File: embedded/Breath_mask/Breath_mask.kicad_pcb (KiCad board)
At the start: 2 copper layers, 38 parts, among them IC1 TPS61291DRVR, J2 USB, J4 Conn_ST_STDC14, SW2 SW_Push, SW3 SW_Push, U1 LPS22HBTR, U23 M95256, U4 STM32L052K8Tx

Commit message: Aggiornamento sbroglio
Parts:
- added G***: LOGO, LOGO, B.Cu at (115.8, 87.8)
- moved TP1 47.8 mm to (137.5, 48.2)
- moved J4 47.1 mm to (147.1, 61.4), turned to 90 degrees
- moved R10 44.4 mm to (117.0, 83.5), turned to 180 degrees
- moved R9 40.6 mm to (120.5, 79.3), turned to -90 degrees
- moved R8 39.4 mm to (117.0, 86.8)
- moved C3 38.9 mm to (126.5, 64.3), turned to -90 degrees
- moved SW3 38.1 mm to (122.8, 73.0)
- moved C11 35.7 mm to (117.0, 79.8)
- moved C8 35.4 mm to (117.8, 74.5), turned to -90 degrees
- moved C6 32.0 mm to (134.8, 63.5), turned to 90 degrees
- moved R7 31.7 mm to (131.8, 64.3)
- moved R15 31.0 mm to (130.0, 80.6), turned to -90 degrees
- moved R12 28.5 mm to (132.0, 80.6), turned to -90 degrees
- moved C4 27.1 mm to (126.6, 68.6)
- moved C5 27.1 mm to (133.3, 60.0)
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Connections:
- SW2 pad 3: (no net) -> GND
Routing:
- net +3V3: track 5.31 -> 178.0 mm
- net Net-(BT1-+): track 0.00 -> 56.5 mm
- net /SENS_CS: track 0.00 -> 41.9 mm, vias 0 -> 4
- net /~{RST}: track 0.00 -> 40.1 mm, vias 0 -> 2
- net /USB_F: track 0.00 -> 32.5 mm, vias 0 -> 2
- net /SPI1_SCK: track 0.00 -> 30.6 mm, vias 0 -> 4
- net /USART1_RX: track 0.00 -> 27.6 mm, vias 0 -> 2
- net /SPI1_MOSI: track 0.00 -> 26.4 mm
- net /SPI1_MISO: track 0.00 -> 24.4 mm, vias 0 -> 2
- net /INTERRUPT_SENS: track 0.00 -> 23.3 mm, vias 0 -> 2
- net Net-(IC1-VIN): track 0.00 -> 21.4 mm, vias 0 -> 2
- net Net-(J2-VBUS-PadA4): track 0.00 -> 20.4 mm
- net /USART1_TX: track 0.00 -> 20.3 mm, vias 0 -> 2
- net Net-(J2-CC2): track 0.00 -> 17.4 mm, vias 0 -> 2
- net /MEM_CS: track 0.00 -> 16.8 mm
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- added copper zone on B.Cu, net GND
- added copper zone on F.Cu, net GND
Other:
- board outline added: 57.8 x 51.2 mm
- board text added: "Anna Dal Mas, Alessia Rinaldi"
- board text added: "Breath Mask Board"
- board text added: "Low-Power Embedded Systems Project"

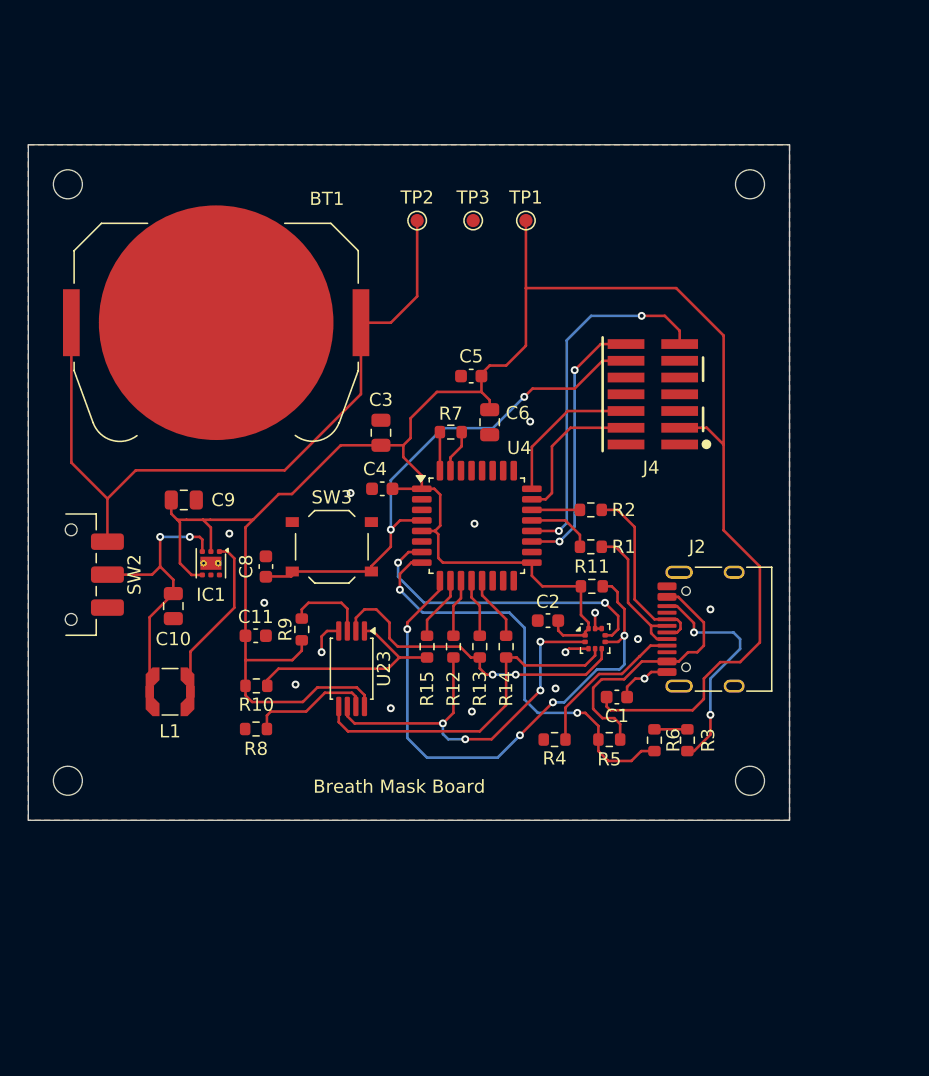
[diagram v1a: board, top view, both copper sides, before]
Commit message: dimensions fixed without traces
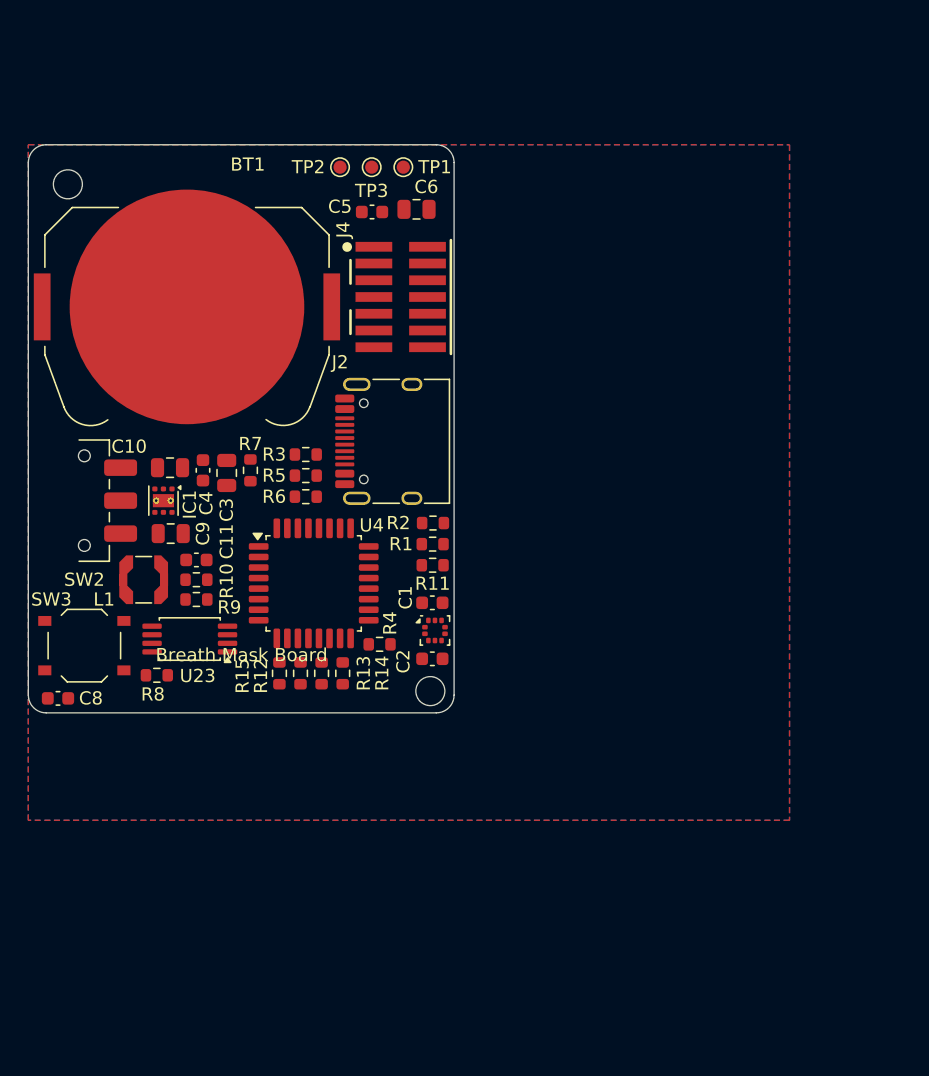
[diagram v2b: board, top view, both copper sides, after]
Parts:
- moved R3 36.2 mm to (120.8, 66.0), turned to 180 degrees
- moved R6 32.3 mm to (120.8, 69.2), turned to 180 degrees
- moved R5 30.5 mm to (120.8, 67.6)
- moved J2 28.3 mm to (127.8, 65.0)
- moved J4 20.5 mm to (128.0, 54.0), turned to -90 degrees
- moved SW3 20.2 mm to (104.0, 80.5)
- moved C8 18.7 mm to (102.0, 84.5), turned to 180 degrees
- moved C6 17.1 mm to (129.2, 47.4), turned to 180 degrees
- moved C1 15.7 mm to (130.4, 77.2)
- moved R7 15.5 mm to (116.6, 67.2), turned to -90 degrees
- moved R4 15.1 mm to (126.4, 80.4)
- moved C5 14.5 mm to (125.8, 47.6)
- moved C4 13.7 mm to (113.0, 67.2), turned to -90 degrees
- moved U4 13.1 mm to (121.4, 75.8)
- moved R14 12.6 mm to (123.6, 82.6)
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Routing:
- net +3V3: track 178.0 -> 0.00 mm
- net Net-(BT1-+): track 56.5 -> 0.00 mm
- net /SENS_CS: track 41.9 -> 0.00 mm, vias 4 -> 0
- net /~{RST}: track 40.1 -> 0.00 mm, vias 2 -> 0
- net /USB_F: track 32.5 -> 0.00 mm, vias 2 -> 0
- net /SPI1_SCK: track 30.6 -> 0.00 mm, vias 4 -> 0
- net /USART1_RX: track 27.6 -> 0.00 mm, vias 2 -> 0
- net /SPI1_MOSI: track 26.4 -> 0.00 mm
- net /SPI1_MISO: track 24.4 -> 0.00 mm, vias 2 -> 0
- net /INTERRUPT_SENS: track 23.3 -> 0.00 mm, vias 2 -> 0
- net Net-(IC1-VIN): track 21.4 -> 0.00 mm, vias 2 -> 0
- net Net-(J2-VBUS-PadA4): track 20.4 -> 0.00 mm
- net /USART1_TX: track 20.3 -> 0.00 mm, vias 2 -> 0
- net Net-(J2-CC2): track 17.4 -> 0.00 mm, vias 2 -> 0
- net /MEM_CS: track 16.8 -> 0.00 mm
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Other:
- board size 57.8 x 51.2 mm -> 32.3 x 43.1 mm

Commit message: Aggiornamento sbroglio con tool
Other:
- board text removed: "Breath Mask Board"
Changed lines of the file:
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@@
 		(layer "Edge.Cuts")
 	)
-	(gr_text "Breath Mask Board"
-		(at 109.4 81.8 0)
-		(layer "F.SilkS")
-		(effects
-			(font
-				(size 1 1)
-				(thickness 0.15)
-			)
-			(justify left bottom)
-		)
-	)
 	(gr_text "Anna Dal Mas, Alessia Rinaldi"
-		(at 127.4 50.8 0)
+		(at 127.090417 52.536382 0)
 		(layer "B.SilkS")
 		(effects
@@
 	)
 	(gr_text "Low-Power Embedded Systems Project"
-		(at 131.2 48.8 0)
+		(at 130.890417 50.536382 0)
 		(layer "B.SilkS")
 		(effects

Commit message: Sbroglio con tool
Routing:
- net +3V3: track 0.00 -> 115.3 mm
- net /~{RST}: track 0.00 -> 56.3 mm, vias 0 -> 3
- net Net-(BT1-+): track 0.00 -> 48.3 mm
- net Net-(J2-CC1): track 0.00 -> 40.7 mm, vias 0 -> 2
- net /SPI1_MOSI: track 0.00 -> 34.6 mm, vias 0 -> 2
- net /SPI1_SCK: track 0.00 -> 28.2 mm, vias 0 -> 3
- net /SWDIO: track 0.00 -> 27.0 mm, vias 0 -> 4
- net /USART1_TX: track 0.00 -> 25.5 mm, vias 0 -> 2
- net /SWCLK: track 0.00 -> 24.4 mm
- net /SPI1_MISO: track 0.00 -> 23.1 mm
- net /USART1_RX: track 0.00 -> 22.1 mm
- net /SENS_CS: track 0.00 -> 21.4 mm, vias 0 -> 2
- net /USB_DM: track 0.00 -> 20.5 mm, vias 0 -> 2
- net /INTERRUPT_SENS: track 0.00 -> 19.4 mm, vias 0 -> 2
- net /USB_F: track 0.00 -> 19.3 mm, vias 0 -> 2
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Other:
- board size 32.3 x 43.1 mm -> 33 x 43.1 mm

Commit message: errors fixed
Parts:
- moved BT1 0.15 mm to (111.9, 54.8)
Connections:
- SW2 pad 3: GND -> (no net)
- U4 pad 2: unconnected-(U4-PC14-Pad2) -> /~{HOLD}
- U4 pad 3: unconnected-(U4-PC15-Pad3) -> /~{W}
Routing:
- net /~{HOLD}: track 3.55 -> 20.7 mm, vias 0 -> 4
- net /~{W}: track 3.73 -> 11.2 mm, vias 0 -> 2
- net GND: track 0.00 -> 2.37 mm, vias 4 -> 70
- net /~{RST}: track 56.3 -> 58.0 mm
- net /INTERRUPT_SENS: track 19.4 -> 17.7 mm
- net +3V3: track 115.3 -> 116.0 mm
- net /SENS_CS: track 21.4 -> 21.9 mm
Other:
- outline, holes or cut-outs redrawn
